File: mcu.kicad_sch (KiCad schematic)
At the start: 14 parts, among them U10 PIC18F24K42, U21 LM4040DBZ-2.0

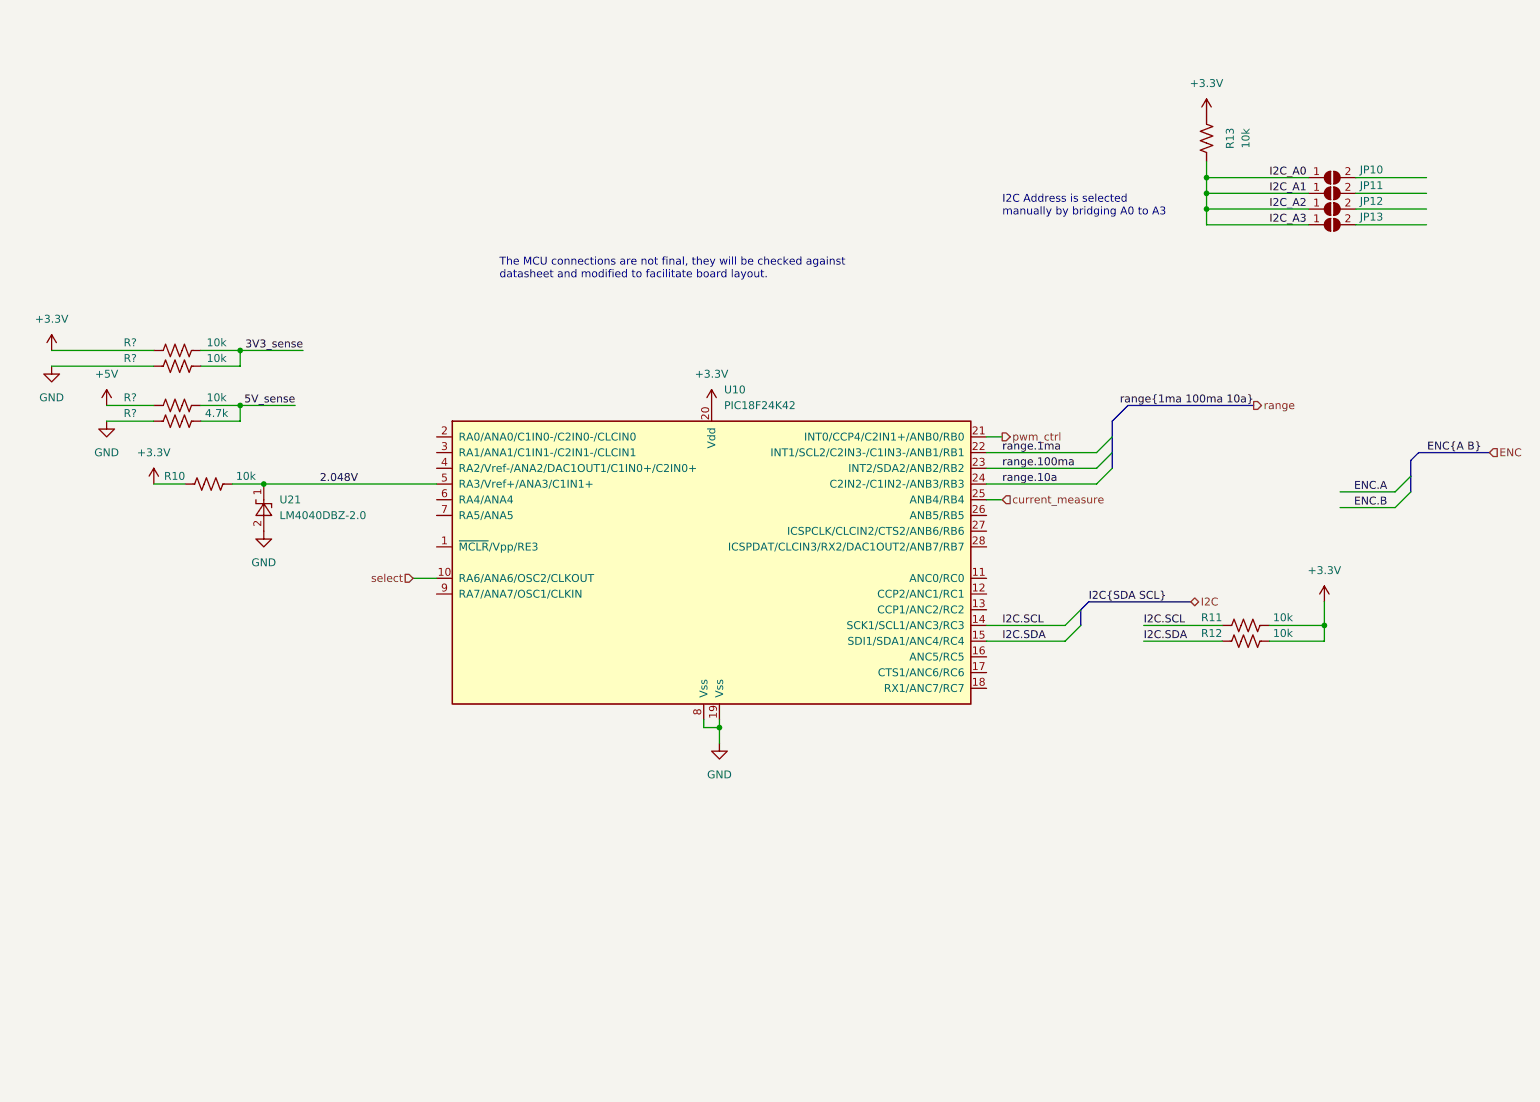
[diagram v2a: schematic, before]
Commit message: Add uart usb controller
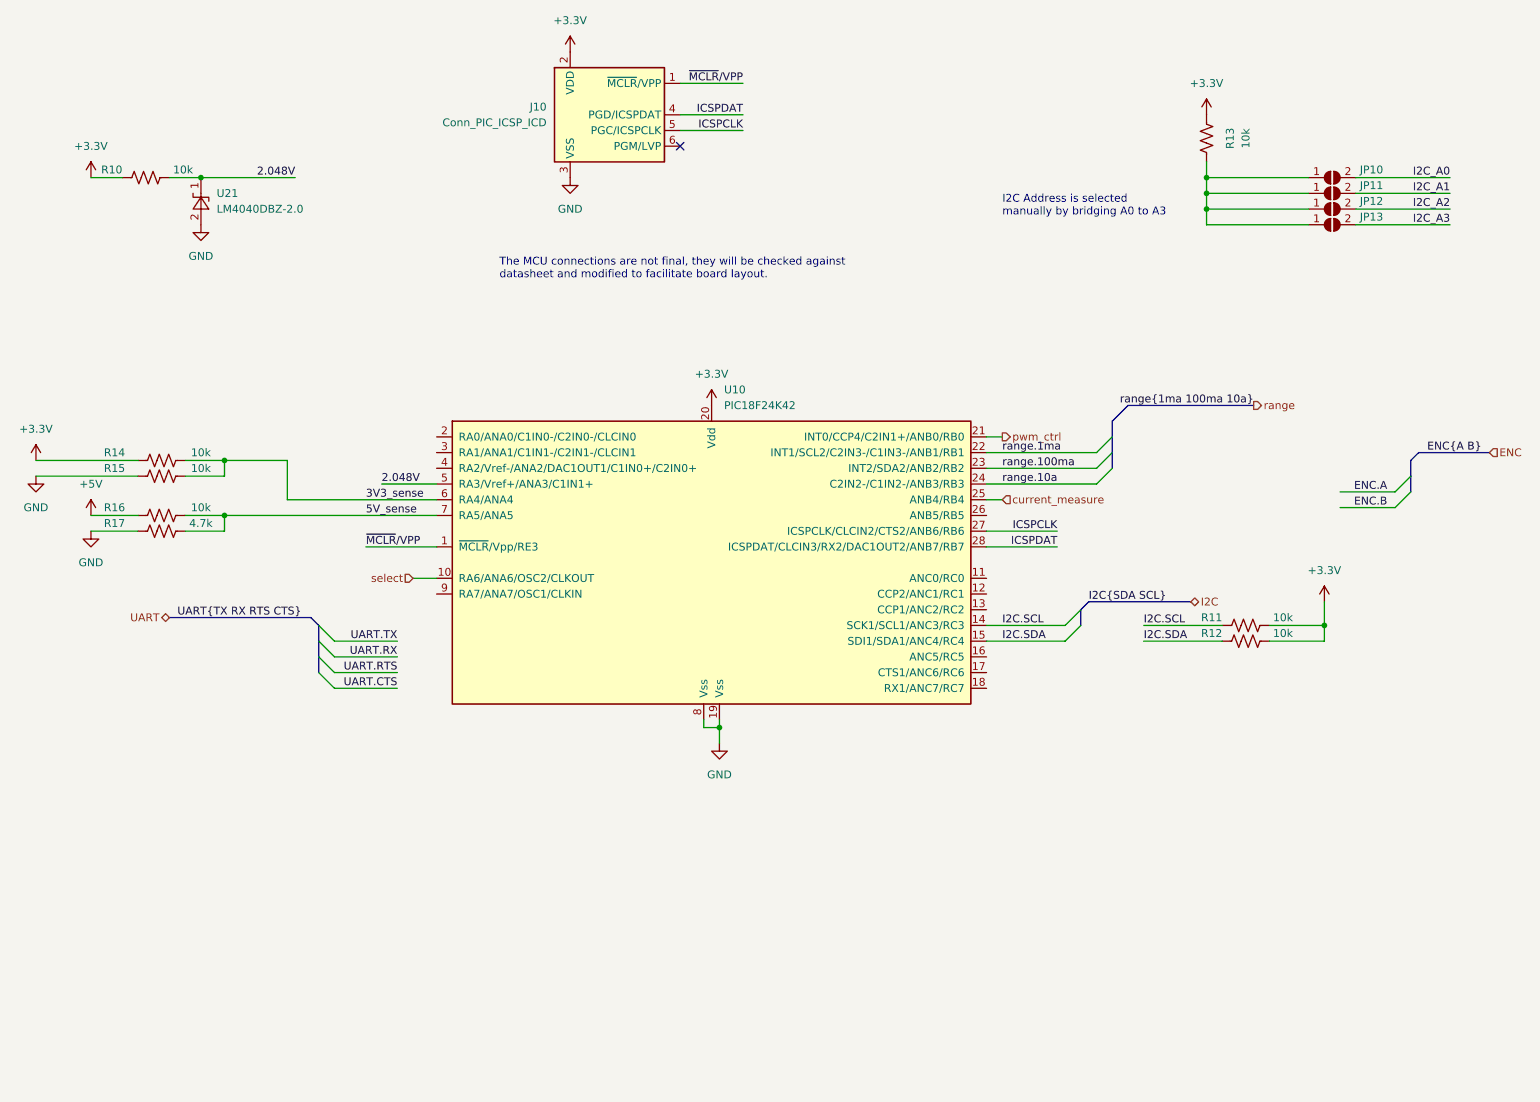
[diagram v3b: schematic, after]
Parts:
- added J10: Conn_PIC_ICSP_ICD, Connector_PinHeader_2.54mm:PinHeader_1x06_P2.54mm_Horizontal, symbol Connector:Conn_PIC_ICSP_ICD
- gave numbers to parts that had none: 4
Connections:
- net +3V3: now also J10.2 (VDD)
- net 3V3_sense: now also U10.6 (RA4/ANA4)
- net 5V_sense: now also U10.7 (RA5/ANA5)
- net GND: now also J10.3 (VSS)
- net I2C_A0: now also JP10.2 (B); no longer JP10.1 (A), JP11.1 (A), JP12.1 (A), JP13.1 (A), R13.1
- net ~{MCLR}/VPP: now reaches U10.1 (~{MCLR}/Vpp/RE3)
- net ~{MCLR}/VPP: now also J10.1 (~{MCLR}/VPP)
- net ICSPCLK: now reaches U10.27 (ICSPCLK/CLCIN2/CTS2/ANB6/RB6)
- net ICSPCLK: now also J10.5 (PGC/ICSPCLK)
- net ICSPDAT: now reaches U10.28 (ICSPDAT/CLCIN3/RX2/DAC1OUT2/ANB7/RB7)
- net ICSPDAT: now also J10.4 (PGD/ICSPDAT)
- net I2C_A2: now reaches JP12.2 (B)
- net I2C_A3: now reaches JP13.2 (B)
- net I2C_A1: now reaches JP11.2 (B)
- new net: JP10.1 (A), JP11.1 (A), JP12.1 (A), JP13.1 (A), R13.1
- no-connect marks 0 -> 1
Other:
- moved on the sheet: R10, R14, R15, R16, R17, U21

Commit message: Fix lots of small things
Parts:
- added C10: 100n, Capacitor_SMD:C_0805_2012Metric, symbol Device:C_Small
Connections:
- net +3V3: now also C10.1
- net ENC.A: now also U10.4 (RA2/Vref-/ANA2/DAC1OUT1/C1IN0+/C2IN0+)
- net ENC.B: now also U10.21 (INT0/CCP4/C2IN1+/ANB0/RB0)
- net GND: now also C10.2
- net UART.CTS: now also U10.17 (CTS1/ANC6/RC6)
- net UART.RTS: now also U10.13 (CCP1/ANC2/RC2)
- net UART.RX: now also U10.18 (RX1/ANC7/RC7)
- net UART.TX: now also U10.16 (ANC5/RC5)
- net pwm_ctrl: now also U10.26 (ANB5/RB5); no longer U10.21 (INT0/CCP4/C2IN1+/ANB0/RB0)
- net select: now also U10.3 (RA1/ANA1/C1IN1-/C2IN1-/CLCIN1); no longer U10.10 (RA6/ANA6/OSC2/CLKOUT)

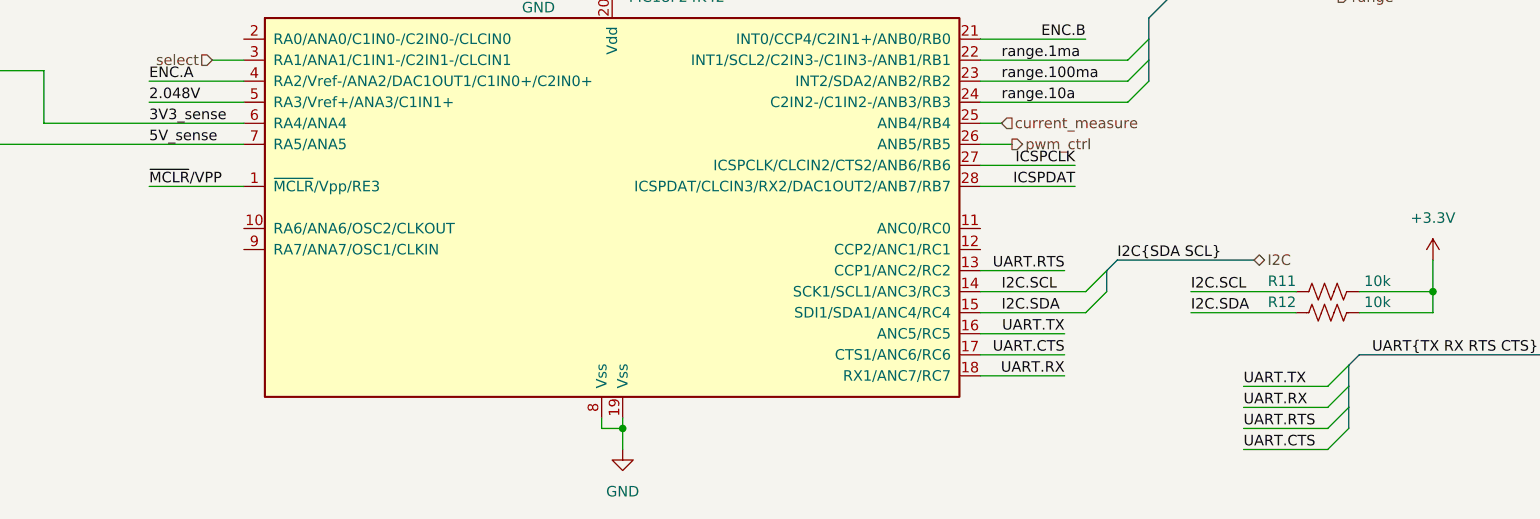
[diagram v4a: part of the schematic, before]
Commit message: Arrange components of subcircuits
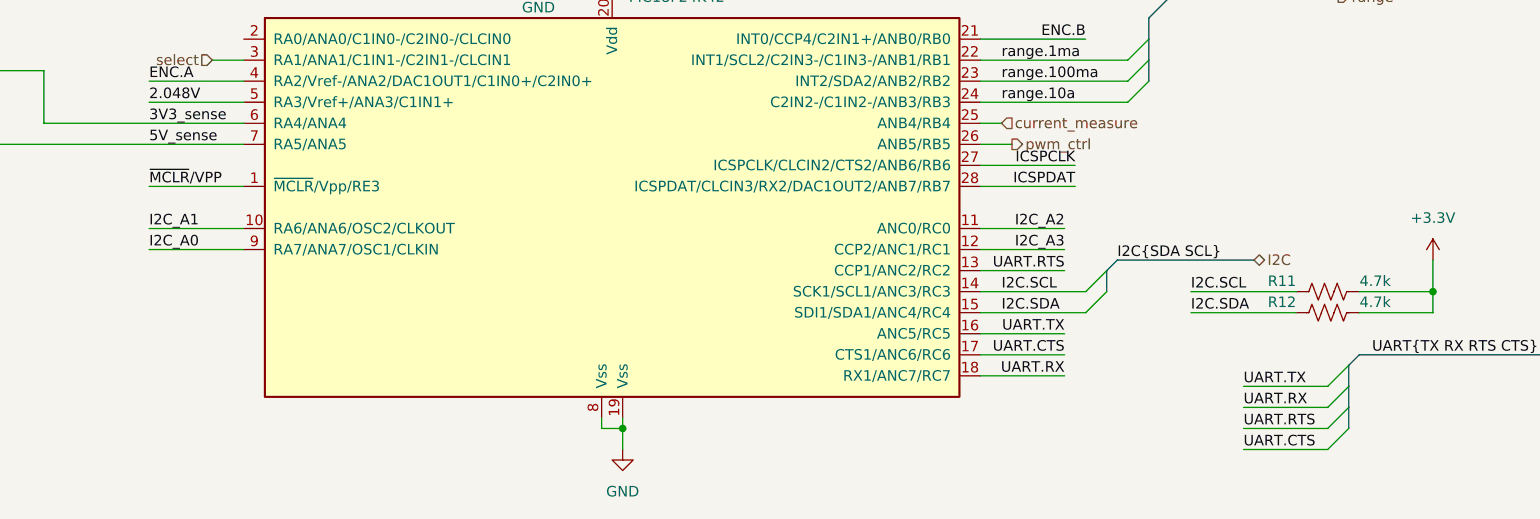
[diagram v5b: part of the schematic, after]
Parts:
- R11, R12: value 10k -> 4.7k
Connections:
- net I2C_A0: now also U10.9 (RA7/ANA7/OSC1/CLKIN)
- net I2C_A1: now also U10.10 (RA6/ANA6/OSC2/CLKOUT)
- net I2C_A2: now also U10.11 (ANC0/RC0)
- net I2C_A3: now also U10.12 (CCP2/ANC1/RC1)
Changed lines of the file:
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@@
+    (stroke (width 0) (type default) (color 0 0 0 0))
+  )
+  (wire (pts (xy 86.36 105.41) (xy 97.79 105.41))
     (stroke (width 0) (type default) (color 0 0 0 0))
   )
@@
     (stroke (width 0) (type default) (color 0 0 0 0))
   )
+  (wire (pts (xy 186.69 105.41) (xy 196.85 105.41))
+    (stroke (width 0) (type default) (color 0 0 0 0))
+  )
   (wire (pts (xy 241.3 115.57) (xy 241.3 113.03))
     (stroke (width 0) (type default) (color 0 0 0 0))
@@
     (stroke (width 0) (type default) (color 0 0 0 0))
   )
+  (wire (pts (xy 86.36 107.95) (xy 97.79 107.95))
+    (stroke (width 0) (type default) (color 0 0 0 0))
+  )
   (wire (pts (xy 140.97 129.54) (xy 143.51 129.54))
     (stroke (width 0) (type default) (color 0 0 0 0))
@@
   )
   (wire (pts (xy 212.09 113.03) (xy 224.79 113.03))
+    (stroke (width 0) (type default) (color 0 0 0 0))
+  )
+  (wire (pts (xy 186.69 107.95) (xy 196.85 107.95))
     (stroke (width 0) (type default) (color 0 0 0 0))
   )
@@
     (effects (font (size 1.27 1.27)) (justify right bottom))
   )
+  (label "I2C_A2" (at 196.85 105.41 180)
+    (effects (font (size 1.27 1.27)) (justify right bottom))
+  )
   (label "range.100ma" (at 189.23 87.63 0)
     (effects (font (size 1.27 1.27)) (justify left bottom))
@@
     (effects (font (size 1.27 1.27)) (justify left bottom))
   )
+  (label "I2C_A0" (at 86.36 107.95 0)
+    (effects (font (size 1.27 1.27)) (justify left bottom))
+  )
   (label "2.048V" (at 74.93 40.64 180)
     (effects (font (size 1.27 1.27)) (justify right bottom))
@@
   )
   (label "UART.RX" (at 196.85 123.19 180)
+    (effects (font (size 1.27 1.27)) (justify right bottom))
+  )
+  (label "I2C_A1" (at 86.36 105.41 0)
+    (effects (font (size 1.27 1.27)) (justify left bottom))
+  )
+  (label "I2C_A3" (at 196.85 107.95 180)
     (effects (font (size 1.27 1.27)) (justify right bottom))
   )
@@
       (effects (font (size 1.27 1.27)) (justify right))
     )
-    (property "Value" "10k" (id 1) (at 236.22 114.3 90)
+    (property "Value" "4.7k" (id 1) (at 236.22 114.3 90)
       (effects (font (size 1.27 1.27)) (justify right))
     )
@@
   (symbol (lib_id "power:GND") (at 133.35 73.66 0) (unit 1)
     (in_bom yes) (on_board yes) (fields_autoplaced)
-    (property "Reference" "#PWR?" (id 0) (at 133.35 80.01 0)
+    (property "Reference" "#PWR0139" (id 0) (at 133.35 80.01 0)
       (effects (font (size 1.27 1.27)) hide)
     )
@@
       (effects (font (size 1.27 1.27)) (justify right))
     )
-    (property "Value" "10k" (id 1) (at 236.22 111.76 90)
-      (effects (font (size 1.27 1.27)) (justify right))
-    )
+    (property "Value" "4.7k" (id 1) (at 236.22 111.76 90)
+      (effects (font (size 1.27 1.27)) (justify right))
+    )

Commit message: WIP PCB Routing + Add load voltage measure
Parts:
- C10: footprint Capacitor_SMD:C_0805_2012Metric -> Capacitor_SMD:C_0402_1005Metric
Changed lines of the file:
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@@
       (effects (font (size 1.27 1.27)) (justify left))
     )
-    (property "Footprint" "Capacitor_SMD:C_0805_2012Metric" (id 2) (at 133.35 71.12 0)
+    (property "Footprint" "Capacitor_SMD:C_0402_1005Metric" (id 2) (at 133.35 71.12 0)
       (effects (font (size 1.27 1.27)) hide)
     )

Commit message: WIP PCB Routing
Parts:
- C10: value 100n -> (none); footprint Capacitor_SMD:C_0402_1005Metric -> (none)
- J10: value Conn_PIC_ICSP_ICD -> (none); footprint Connector_PinHeader_2.54mm:PinHeader_1x06_P2.54mm_Horizontal -> (none)
- JP10, JP11, JP12, JP13: value SolderJumper_2_Open -> (none); footprint Jumper:SolderJumper-2_P1.3mm_Open_TrianglePad1.0x1.5mm -> (none)
- R10, R13, R14, R15, R16: value 10k -> (none); footprint Resistor_SMD:R_0805_2012Metric -> (none)
- R11, R12, R17: value 4.7k -> (none); footprint Resistor_SMD:R_0805_2012Metric -> (none)
- U10: value PIC18F24K42 -> (none); footprint Package_SO:SSOP-28_5.3x10.2mm_P0.65mm -> (none)
- U11: renamed from U21; value LM4040DBZ-2.0 -> (none); footprint Package_TO_SOT_SMD:SOT-23 -> (none)
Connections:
- net 3V3_sense: now also U10.16 (ANC5/RC5); no longer U10.6 (RA4/ANA4)
- net 5V_sense: now also U10.17 (CTS1/ANC6/RC6); no longer U10.7 (RA5/ANA5)
- net ENC.A: now also U10.12 (CCP2/ANC1/RC1); no longer U10.4 (RA2/Vref-/ANA2/DAC1OUT1/C1IN0+/C2IN0+)
- net ENC.B: now also U10.11 (ANC0/RC0); no longer U10.21 (INT0/CCP4/C2IN1+/ANB0/RB0)
- net I2C_A0: now also U10.6 (RA4/ANA4); no longer U10.9 (RA7/ANA7/OSC1/CLKIN)
- net I2C_A1: now also U10.7 (RA5/ANA5); no longer U10.10 (RA6/ANA6/OSC2/CLKOUT)
- net I2C_A2: now also U10.9 (RA7/ANA7/OSC1/CLKIN); no longer U10.11 (ANC0/RC0)
- net I2C_A3: now also U10.10 (RA6/ANA6/OSC2/CLKOUT); no longer U10.12 (CCP2/ANC1/RC1)
- net UART.CTS: now also U10.22 (INT1/SCL2/C2IN3-/C1IN3-/ANB1/RB1); no longer U10.17 (CTS1/ANC6/RC6)
- net UART.RTS: now also U10.18 (RX1/ANC7/RC7); no longer U10.13 (CCP1/ANC2/RC2)
- net UART.RX: now also U10.23 (INT2/SDA2/ANB2/RB2); no longer U10.18 (RX1/ANC7/RC7)
- net UART.TX: now also U10.21 (INT0/CCP4/C2IN1+/ANB0/RB0); no longer U10.16 (ANC5/RC5)
- net range.100ma: now also U10.24 (C2IN2-/C1IN2-/ANB3/RB3); no longer U10.23 (INT2/SDA2/ANB2/RB2)
- net range.10a: no longer U10.24 (C2IN2-/C1IN2-/ANB3/RB3)
- net range.1ma: no longer U10.22 (INT1/SCL2/C2IN3-/C1IN3-/ANB1/RB1)
- net select: now also U10.13 (CCP1/ANC2/RC2); no longer U10.3 (RA1/ANA1/C1IN1-/C2IN1-/CLCIN1)
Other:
- moved on the sheet: R14, R15, R16, R17
